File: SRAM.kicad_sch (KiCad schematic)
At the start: 5 parts, among them U7 23LC1024-I/SN

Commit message: (sch) relabel
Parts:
- renumbered U7 to U1201
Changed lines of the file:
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@@
         )
         (path "/4185c36c-c66e-4dbd-be5d-841e551f4885/ec9450dd-98d1-46b3-b2f6-66ba91725bce"
-          (reference "R59") (unit 1)
+          (reference "R1202") (unit 1)
         )
       )
@@
         )
         (path "/4185c36c-c66e-4dbd-be5d-841e551f4885/ec9450dd-98d1-46b3-b2f6-66ba91725bce"
-          (reference "#PWR0208") (unit 1)
+          (reference "#PWR01203") (unit 1)
         )
       )
@@
         )
         (path "/4185c36c-c66e-4dbd-be5d-841e551f4885/ec9450dd-98d1-46b3-b2f6-66ba91725bce"
-          (reference "#PWR0209") (unit 1)
+          (reference "#PWR01202") (unit 1)
         )
       )
@@
         )
         (path "/4185c36c-c66e-4dbd-be5d-841e551f4885/ec9450dd-98d1-46b3-b2f6-66ba91725bce"
-          (reference "#PWR0205") (unit 1)
+          (reference "#PWR01206") (unit 1)
         )
       )
@@
         )
         (path "/4185c36c-c66e-4dbd-be5d-841e551f4885/ec9450dd-98d1-46b3-b2f6-66ba91725bce"
-          (reference "R37") (unit 1)
+          (reference "R1203") (unit 1)
         )
       )
@@
         )
         (path "/4185c36c-c66e-4dbd-be5d-841e551f4885/ec9450dd-98d1-46b3-b2f6-66ba91725bce"
-          (reference "#PWR0211") (unit 1)
+          (reference "#PWR01205") (unit 1)
         )
       )
@@
         )
         (path "/4185c36c-c66e-4dbd-be5d-841e551f4885/ec9450dd-98d1-46b3-b2f6-66ba91725bce"
-          (reference "CB14") (unit 1)
+          (reference "CB1201") (unit 1)
         )
       )
@@
         )
         (path "/4185c36c-c66e-4dbd-be5d-841e551f4885/ec9450dd-98d1-46b3-b2f6-66ba91725bce"
-          (reference "#PWR0210") (unit 1)
+          (reference "#PWR01201") (unit 1)
         )
       )
@@
   (symbol (lib_id "grootvoet:SRAM_23LC1024") (at 117.475 102.87 0) (unit 1)
     (in_bom yes) (on_board yes) (dnp no) (fields_autoplaced)
-    (property "Reference" "U7" (at 119.4309 88.9 0)
+    (property "Reference" "U1201" (at 119.4309 88.9 0)
       (effects (font (size 1.27 1.27)) (justify left))
     )
@@
       (project "kleinvoet"
         (path "/4185c36c-c66e-4dbd-be5d-841e551f4885/ec9450dd-98d1-46b3-b2f6-66ba91725bce"
-          (reference "U7") (unit 1)
+          (reference "U1201") (unit 1)
         )
       )
@@
         )
         (path "/4185c36c-c66e-4dbd-be5d-841e551f4885/ec9450dd-98d1-46b3-b2f6-66ba91725bce"
-          (reference "#PWR0207") (unit 1)
+          (reference "#PWR01204") (unit 1)
         )
       )
@@
         )
         (path "/4185c36c-c66e-4dbd-be5d-841e551f4885/ec9450dd-98d1-46b3-b2f6-66ba91725bce"
-          (reference "R61") (unit 1)
+          (reference "R1201") (unit 1)
         )
       )
@@
         )
         (path "/4185c36c-c66e-4dbd-be5d-841e551f4885/ec9450dd-98d1-46b3-b2f6-66ba91725bce"
-          (reference "#PWR0206") (unit 1)
-        )
-      )
+          (reference "#PWR01207") (unit 1)
+        )
+      )

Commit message: (hk) asign footprints
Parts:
- renumbered U1201 to U1301
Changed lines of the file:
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@@
         )
         (path "/4185c36c-c66e-4dbd-be5d-841e551f4885/ec9450dd-98d1-46b3-b2f6-66ba91725bce"
-          (reference "R1202") (unit 1)
+          (reference "R1302") (unit 1)
         )
       )
@@
         )
         (path "/4185c36c-c66e-4dbd-be5d-841e551f4885/ec9450dd-98d1-46b3-b2f6-66ba91725bce"
-          (reference "#PWR01203") (unit 1)
+          (reference "#PWR01303") (unit 1)
         )
       )
@@
         )
         (path "/4185c36c-c66e-4dbd-be5d-841e551f4885/ec9450dd-98d1-46b3-b2f6-66ba91725bce"
-          (reference "#PWR01202") (unit 1)
+          (reference "#PWR01302") (unit 1)
         )
       )
@@
         )
         (path "/4185c36c-c66e-4dbd-be5d-841e551f4885/ec9450dd-98d1-46b3-b2f6-66ba91725bce"
-          (reference "#PWR01206") (unit 1)
+          (reference "#PWR01306") (unit 1)
         )
       )
@@
         )
         (path "/4185c36c-c66e-4dbd-be5d-841e551f4885/ec9450dd-98d1-46b3-b2f6-66ba91725bce"
-          (reference "R1203") (unit 1)
+          (reference "R1303") (unit 1)
         )
       )
@@
         )
         (path "/4185c36c-c66e-4dbd-be5d-841e551f4885/ec9450dd-98d1-46b3-b2f6-66ba91725bce"
-          (reference "#PWR01205") (unit 1)
+          (reference "#PWR01305") (unit 1)
         )
       )
@@
         )
         (path "/4185c36c-c66e-4dbd-be5d-841e551f4885/ec9450dd-98d1-46b3-b2f6-66ba91725bce"
-          (reference "CB1201") (unit 1)
+          (reference "CB1301") (unit 1)
         )
       )
@@
         )
         (path "/4185c36c-c66e-4dbd-be5d-841e551f4885/ec9450dd-98d1-46b3-b2f6-66ba91725bce"
-          (reference "#PWR01201") (unit 1)
+          (reference "#PWR01301") (unit 1)
         )
       )
@@
   (symbol (lib_id "grootvoet:SRAM_23LC1024") (at 117.475 102.87 0) (unit 1)
     (in_bom yes) (on_board yes) (dnp no) (fields_autoplaced)
-    (property "Reference" "U1201" (at 119.4309 88.9 0)
+    (property "Reference" "U1301" (at 119.4309 88.9 0)
       (effects (font (size 1.27 1.27)) (justify left))
     )
@@
       (project "kleinvoet"
         (path "/4185c36c-c66e-4dbd-be5d-841e551f4885/ec9450dd-98d1-46b3-b2f6-66ba91725bce"
-          (reference "U1201") (unit 1)
+          (reference "U1301") (unit 1)
         )
       )
@@
         )
         (path "/4185c36c-c66e-4dbd-be5d-841e551f4885/ec9450dd-98d1-46b3-b2f6-66ba91725bce"
-          (reference "#PWR01204") (unit 1)
+          (reference "#PWR01304") (unit 1)
         )
       )
@@
         )
         (path "/4185c36c-c66e-4dbd-be5d-841e551f4885/ec9450dd-98d1-46b3-b2f6-66ba91725bce"
-          (reference "R1201") (unit 1)
+          (reference "R1301") (unit 1)
         )
       )
@@
         )
         (path "/4185c36c-c66e-4dbd-be5d-841e551f4885/ec9450dd-98d1-46b3-b2f6-66ba91725bce"
-          (reference "#PWR01207") (unit 1)
-        )
-      )
+          (reference "#PWR01307") (unit 1)
+        )
+      )

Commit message: (sch) change passives to 0402
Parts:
- R1: footprint Resistor_SMD:R_0603_1608Metric_Pad0.98x0.95mm_HandSolder -> Resistor_SMD:R_0402_1005Metric; MPN RC0603JR-0710KL -> RT0402FRE1310KL
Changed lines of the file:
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@@
       (effects (font (size 1.27 1.27)) (justify left))
     )
-    (property "Footprint" "Resistor_SMD:R_0603_1608Metric_Pad0.98x0.95mm_HandSolder" (at 100.965 96.52 0)
+    (property "Footprint" "Resistor_SMD:R_0402_1005Metric" (at 100.965 96.52 0)
       (effects (font (size 1.27 1.27)) hide)
     )
@@
       (effects (font (size 1.27 1.27)) hide)
     )
-    (property "MPN" "RC0603JR-0710KL" (at 100.965 96.52 0)
+    (property "MPN" "RT0402FRE1310KL" (at 100.965 96.52 0)
       (effects (font (size 1.27 1.27)) hide)
     )
@@
       (effects (font (size 1.27 1.27)) (justify left))
     )
-    (property "Footprint" "Resistor_SMD:R_0603_1608Metric_Pad0.98x0.95mm_HandSolder" (at 147.955 102.235 0)
+    (property "Footprint" "Resistor_SMD:R_0402_1005Metric" (at 147.955 102.235 0)
       (effects (font (size 1.27 1.27)) hide)
     )
@@
       (effects (font (size 1.27 1.27)) hide)
     )
-    (property "MPN" "RC0603JR-0710KL" (at 147.955 102.235 0)
+    (property "MPN" "RT0402FRE1310KL" (at 147.955 102.235 0)
       (effects (font (size 1.27 1.27)) hide)
     )
@@
       (effects (font (size 1.27 1.27)) (justify left))
     )
-    (property "Footprint" "Resistor_SMD:R_0603_1608Metric_Pad0.98x0.95mm_HandSolder" (at 91.44 96.52 0)
+    (property "Footprint" "Resistor_SMD:R_0402_1005Metric" (at 91.44 96.52 0)
       (effects (font (size 1.27 1.27)) hide)
     )
@@
       (effects (font (size 1.27 1.27)) hide)
     )
-    (property "MPN" "RC0603JR-0710KL" (at 91.44 96.52 0)
-      (effects (font (size 1.27 1.27)) hide)
-    )
+    (property "MPN" "RT0402FRE1310KL" (at 91.44 96.52 0)
+      (effects (font (size 1.27 1.27)) hide)
+    )

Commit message: (pcb) initial layout
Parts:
- CB1: footprint Capacitor_SMD:C_0603_1608Metric_Pad1.08x0.95mm_HandSolder -> Capacitor_SMD:C_0402_1005Metric; MPN C0603C104M5RACTU -> C0402C104K8PACTU
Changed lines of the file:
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@@
       (effects (font (size 1.27 1.27)) (justify left))
     )
-    (property "Footprint" "Capacitor_SMD:C_0603_1608Metric_Pad1.08x0.95mm_HandSolder" (at 182.88 104.14 0)
+    (property "Footprint" "Capacitor_SMD:C_0402_1005Metric" (at 182.88 104.14 0)
       (effects (font (size 1.27 1.27)) hide)
     )
@@
       (effects (font (size 1.27 1.27)) hide)
     )
-    (property "MPN" "C0603C104M5RACTU" (at 182.88 104.14 0)
+    (property "MPN" "C0402C104K8PACTU" (at 182.88 104.14 0)
       (effects (font (size 1.27 1.27)) hide)
     )

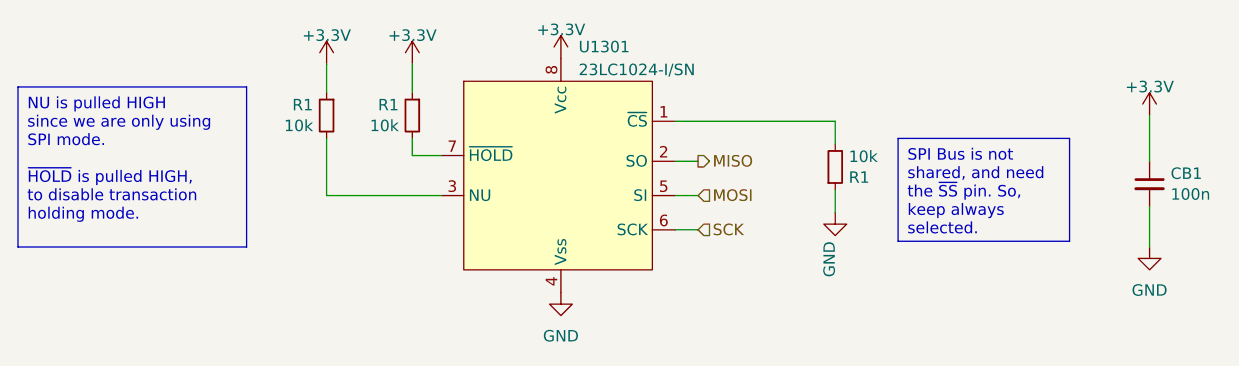
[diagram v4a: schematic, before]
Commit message: (sch) change to 100k pull-ups
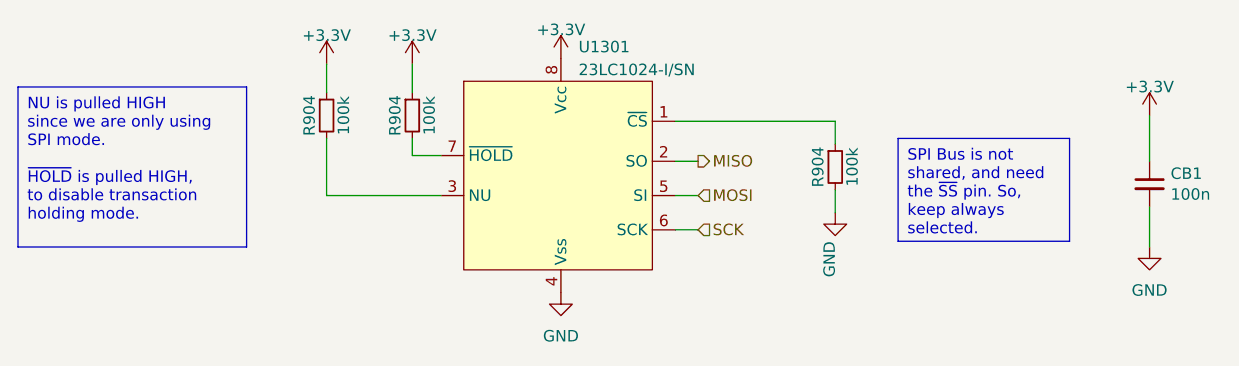
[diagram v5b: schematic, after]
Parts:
- removed R1 (x3): 10k, Resistor_SMD:R_0402_1005Metric, symbol Device:R_Small
- added R904 (x3): 100k, Resistor_SMD:R_0402_1005Metric, symbol Device:R_Small
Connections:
- net +3.3V: now also R904.1, R904.1
- net GND: now also R904.2
- net at U1301.7 (~{HOLD}): now also R904.2
- net at U1301.1 (~{CS}): now also R904.1
- net at U1301.3 (NU): now also R904.2

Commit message: (sch) update title block
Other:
- company: (none) -> Department of Electrical and Electronic Engineering - Stellenbosch University
- title: (none) -> Kleinvoet
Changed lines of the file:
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@@
 (kicad_sch (version 20230121) (generator eeschema)
   (paper "A4")
+  (title_block
+    (title "Kleinvoet")
+    (date "2023-04-12")
+    (rev "C")
+    (company "Department of Electrical and Electronic Engineering - Stellenbosch University")
+    (comment 1 "Digital Signal Processing Laboratory")
+    (comment 2 "Author: CM Geldenhuys <cmgeldenhuys@sun.ac.za>")
+    (comment 3 "Project: Kleinvoet")
+    (comment 4 "License: CERN-OHL-S-2.0")
+  )
   (wire (pts (xy 130.175 105.41) (xy 132.715 105.41))
     (stroke (width 0) (type default))
